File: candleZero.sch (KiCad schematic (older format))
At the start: 25 parts, among them J1 CONN_02X02, J5 CONN_02X05, J6 DB9_MALE, U1 STM32F072C8Ux, U2 TLV70233DBV, U3 TJA1051TK/3

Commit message: v0.2
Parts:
- removed J1: CONN_02X02, Pin_Headers:Pin_Header_Straight_2x02_Pitch1.27mm, symbol CONN_02X02
- added J1, J2, J3, J4: TEST_1P, pins:Pin_Header_Straight_1x01_Pitch2.00mm, symbol TEST_1P
- J6: footprint Connectors:DB9M_CI -> subd9-small:DB9M_CI_SMALL
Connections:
- net +5V: now also J1.1
- net GND: now also J5.7 (P7), J2.1
- net USB_DM: now also J3.1
- net USB_DP: now also J4.1
- net CAN_L: now reaches J6.2, R4.2, U3.6 (CANL)
- net CAN_H: now reaches J6.7, R4.1, U3.7 (CANH)
- no-connect marks 38 -> 37

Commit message: v0.3
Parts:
- removed D1, D2, D3: LED, LEDs:LED_0603, symbol LED
- removed R1: dnp, Resistors_SMD:R_0603, symbol R
- added D1: LED_RGB, LEDs:LED_RGB_PLCC-6, symbol LED_RGB
- J5: footprint Pin_Headers:Pin_Header_Straight_2x05_Pitch1.27mm -> jtag:Pin_Header_Straight_2x05_Pitch1.27mm
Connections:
- net GND: now also U1.18 (PB0), U1.19 (PB1), U1.20 (PB2), U1.21 (PB10), U1.22 (PB11), U1.25 (PB12), U1.26 (PB13), U1.27 (PB14), U1.28 (PB15), U1.29 (PA8), U1.30 (PA9), U1.31 (PA10), U1.38 (PA15), U1.39 (PB3), U1.40 (PB4), U1.41 (PB5), U1.42 (PB6), U1.43 (PB7)
- net BOOT: now reaches R2.1, U1.44 (BOOT0)
- net at R5.2: now also D1.6 (RA)
- net at R6.2: now also D1.5 (GA)
- net at R7.2: now also D1.4 (BA)
- net LED_R: now reaches U1.12 (PA2)
- net LED_R: now also D1.1 (RK)
- net LED_G: now reaches U1.13 (PA3)
- net LED_G: now also D1.2 (GK)
- net LED_B: now reaches U1.15 (PA5)
- net LED_B: now also D1.3 (BK)
- net LED1: no longer names the net of U1.10 (PA0)
- net LED2: no longer names the net of U1.11 (PA1)
- no-connect marks 37 -> 18
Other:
- moved on the sheet: R2, R5, R6, R7

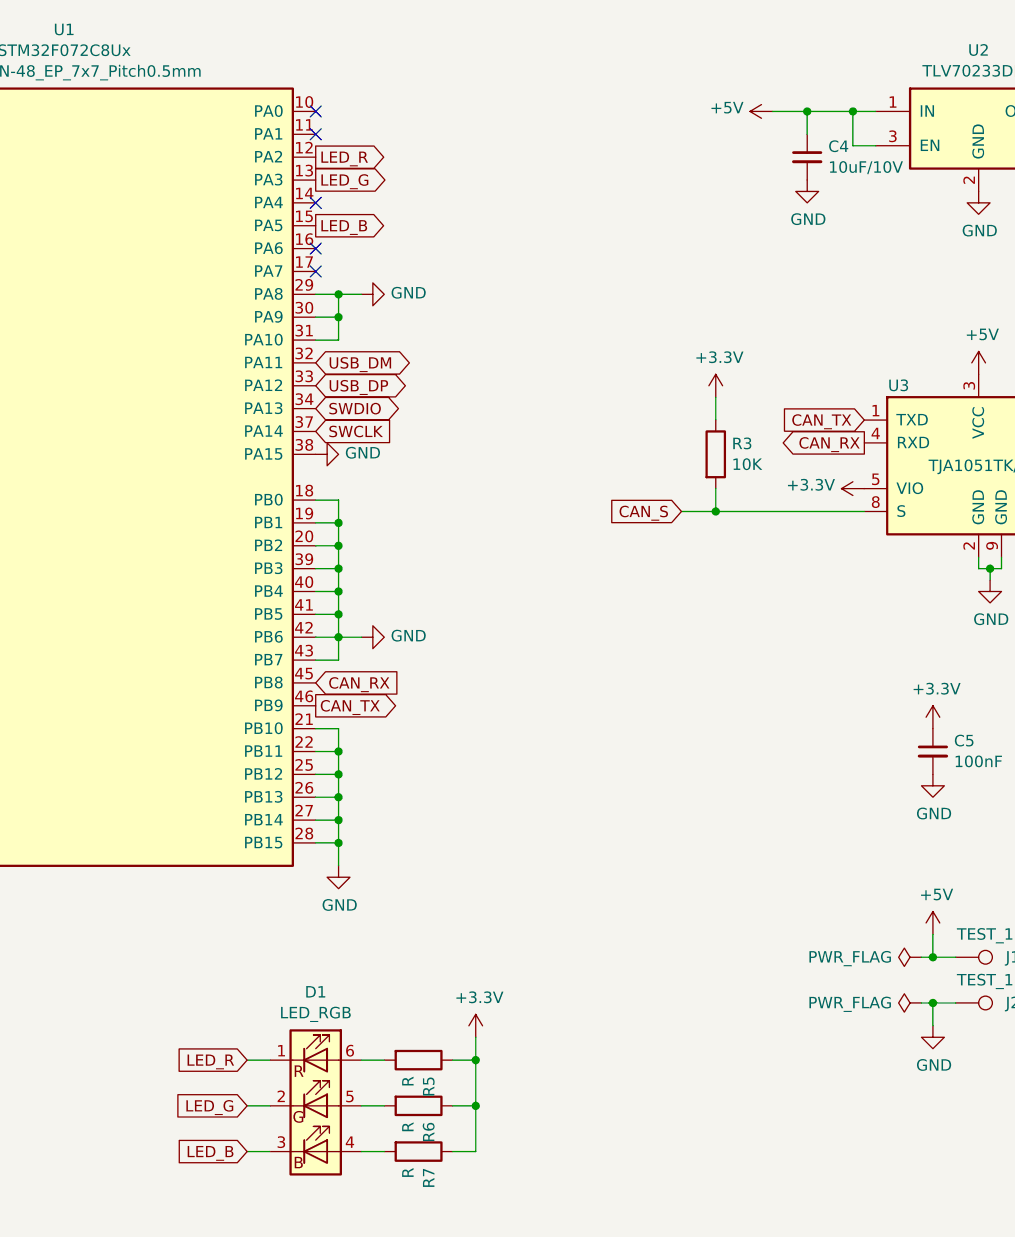
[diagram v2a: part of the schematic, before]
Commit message: fix led colors
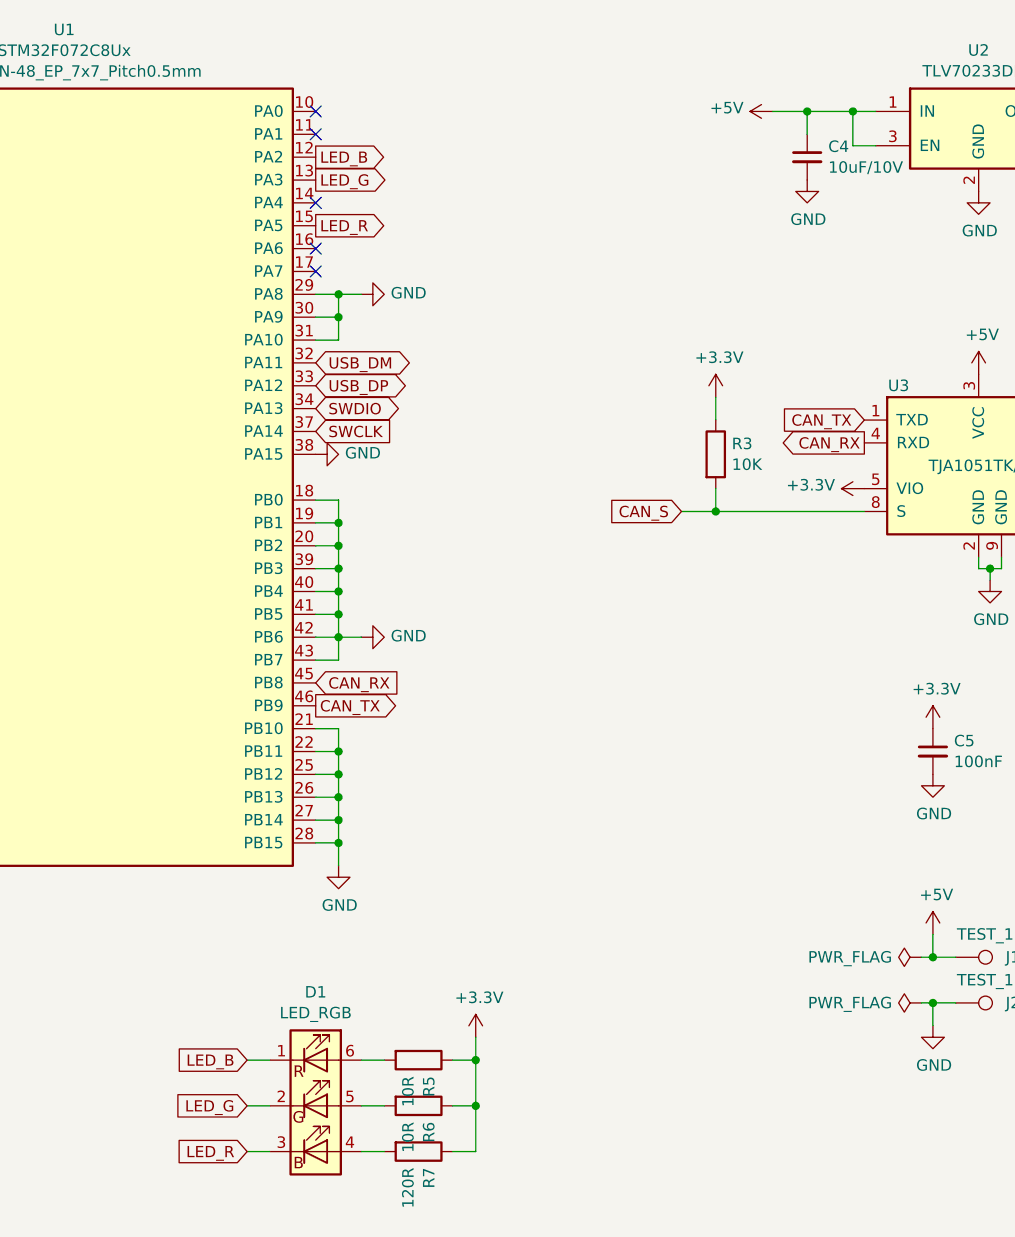
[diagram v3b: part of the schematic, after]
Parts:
- R5, R6: value R -> 10R
- R7: value R -> 120R
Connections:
- net LED_B: now also D1.1 (RK), U1.12 (PA2); no longer D1.3 (BK), U1.15 (PA5)
- net LED_R: now also D1.3 (BK), U1.15 (PA5); no longer D1.1 (RK), U1.12 (PA2)
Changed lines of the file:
@@
 	7050 2000 6950 2000
 Wire Wire Line
-	6950 2000 6950 1850
+	6950 1850 6950 2000
 Wire Wire Line
 	6600 1850 7050 1850
@@
 P 5050 6000
 F 0 "R5" H 5120 6046 50  0000 L CNN
-F 1 "R" H 5120 5955 50  0000 L CNN
+F 1 "10R" H 5120 5955 50  0000 L CNN
 F 2 "Resistors_SMD:R_0603" V 4980 6000 50  0001 C CNN
 F 3 "" H 5050 6000 50  0001 C CNN
@@
 P 5050 6200
 F 0 "R6" H 5120 6246 50  0000 L CNN
-F 1 "R" H 5120 6155 50  0000 L CNN
+F 1 "10R" H 5120 6155 50  0000 L CNN
 F 2 "Resistors_SMD:R_0603" V 4980 6200 50  0001 C CNN
 F 3 "" H 5050 6200 50  0001 C CNN
@@
 P 5050 6400
 F 0 "R7" H 5120 6446 50  0000 L CNN
-F 1 "R" H 5120 6355 50  0000 L CNN
+F 1 "120R" H 5120 6355 50  0000 L CNN
 F 2 "Resistors_SMD:R_0603" V 4980 6400 50  0001 C CNN
 F 3 "" H 5050 6400 50  0001 C CNN
@@
 	5300 6400 5200 6400
 Connection ~ 5300 6200
-Text GLabel 4600 2050 2    49   Output ~ 0
+Text GLabel 4600 2350 2    49   Output ~ 0
 LED_R
 Text GLabel 4600 2150 2    49   Output ~ 0
 LED_G
-Text GLabel 4600 2350 2    49   Output ~ 0
+Text GLabel 4600 2050 2    49   Output ~ 0
 LED_B
 $Comp
@@
 $EndComp
 Text GLabel 4300 6000 0    49   Input ~ 0
-LED_R
+LED_B
 Text GLabel 4300 6200 0    49   Input ~ 0
 LED_G
 Text GLabel 4300 6400 0    49   Input ~ 0
-LED_B
+LED_R
 Wire Wire Line
 	4300 6000 4400 6000
@@
 $EndComp
 Wire Wire Line
-	4800 4150 4600 4150
+	4600 4150 4800 4150
 Wire Wire Line
 	4700 3550 4700 4250
@@
 Connection ~ 4700 4650
 $Comp
-L GND #PWR?
+L GND #PWR039
 U 1 1 59186DDC
 P 4800 2650
-F 0 "#PWR?" H 4800 2400 50  0001 C CNN
+F 0 "#PWR039" H 4800 2400 50  0001 C CNN
 F 1 "GND" V 4805 2522 50  0000 R CNN
 F 2 "" H 4800 2650 50  0001 C CNN
@@
 $EndComp
 Wire Wire Line
-	4800 2650 4600 2650
+	4600 2650 4800 2650
 Wire Wire Line
 	4700 2650 4700 2850

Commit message: v0.5 / bga design test
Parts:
- removed C1, C2, C3, C5, C6, C8, C9: 100nF, Capacitors_SMD:C_0603, symbol C_Small
- removed C4: 10uF/10V, Capacitors_SMD:C_0805, symbol C_Small
- removed C7: 10uF, Capacitors_SMD:C_0805, symbol C_Small
- removed D1: LED_RGB, LEDs:LED_RGB_PLCC-6, symbol LED_RGB
- removed J1, J2, J3, J4: TEST_1P, pins:Pin_Header_Straight_1x01_Pitch2.00mm, symbol TEST_1P
- removed J5: CONN_02X05, jtag:Pin_Header_Straight_2x05_Pitch1.27mm, symbol CONN_02X05
- removed J6: DB9_MALE, subd9-small:DB9M_CI_SMALL, symbol DB9_MALE
- removed R2, R3: 10K, Resistors_SMD:R_0603, symbol R
- removed R4: dnp, Resistors_SMD:R_0805, symbol R
- removed R5, R6: 10R, Resistors_SMD:R_0603, symbol R
- removed R7: 120R, Resistors_SMD:R_0603, symbol R
- removed U1: STM32F072C8Ux, qfn48:QFN-48_EP_7x7_Pitch0.5mm, symbol STM32F072C8Ux
- removed U2: TLV70233DBV, TO_SOT_Packages_SMD:SOT-23-5, symbol TLV70233DBV
- removed U3: TJA1051TK/3, Housings_DFN_QFN:DFN-8-1EP_3x3mm_Pitch0.65mm, symbol TJA1051TK/3
- added C1, C10, C2, C3, C4, C5, C6, C8: 100nF, Capacitor_SMD:C_0603_1608Metric, symbol Device:C_Small
- added C11, C7, C9: 1uF, Capacitor_SMD:C_0603_1608Metric, symbol Device:C_Small
- added D1: LED_RGB, LED_SMD:LED_RGB_PLCC-6, symbol Device:LED_RGB
- added J1: DB9_Male, Connector_Dsub:DSUB-9_Male_EdgeMount_P2.77mm, symbol Connector:DB9_Male
- added R1, R2, R3: R, Resistor_SMD:R_0603_1608Metric, symbol Device:R
- added R5, R6: 10k, Resistor_SMD:R_0603_1608Metric, symbol Device:R_Small
- added TP1: D-, TestPoint:TestPoint_THTPad_1.5x1.5mm_Drill0.7mm, symbol Connector:Test_Point
- added TP2: D+, TestPoint:TestPoint_THTPad_1.5x1.5mm_Drill0.7mm, symbol Connector:Test_Point
- added TP3: +5V, TestPoint:TestPoint_THTPad_1.5x1.5mm_Drill0.7mm, symbol Connector:Test_Point
- added TP4: GND, TestPoint:TestPoint_THTPad_1.5x1.5mm_Drill0.7mm, symbol Connector:Test_Point
- added TP5: VCC, TestPoint:TestPoint_Pad_D1.0mm, symbol Connector:Test_Point
- added TP6: RESET, TestPoint:TestPoint_Pad_D1.0mm, symbol Connector:Test_Point
- added TP7: SWDIO, TestPoint:TestPoint_Pad_D1.0mm, symbol Connector:Test_Point
- added TP8: SWCLK, TestPoint:TestPoint_Pad_D1.0mm, symbol Connector:Test_Point
- added TP9: GND, TestPoint:TestPoint_Pad_D1.0mm, symbol Connector:Test_Point
- added U1: STM32F072RBHx, Package_BGA:UFBGA-64_5x5mm_Layout8x8_P0.5mm, symbol MCU_ST_STM32F0:STM32F072RBHx
- added U2: TJA1051T-3, Package_DFN_QFN:DFN-8_2x2mm_P0.5mm, symbol Interface_CAN_LIN:TJA1051T-3
- added U3: TLV70233_SOT23-5, Package_TO_SOT_SMD:SOT-23-5, symbol Regulator_Linear:TLV70233_SOT23-5
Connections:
- net labels added: +3V3, B, BOOT0, D+, D-, G, R, RESET, RXD, SILENT, TXD
- net labels removed: +3.3V, BOOT, CAN_H, CAN_L, CAN_RX, CAN_S, CAN_TX, LED_B, LED_G, LED_R, NRST, USB_DM, USB_DP
- wire segments 75 -> 87
- no-connect marks 18 -> 36
